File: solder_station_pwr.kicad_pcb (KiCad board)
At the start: 2 copper layers, 82.8 x 69.1 mm, 31 parts, among them J1 PWR_MAIN_LINE, J2 FB_OUT, J3 Conn_01x04, J4 FB_IN, J6 Conn_01x03, Q3 2SD669, T1 RingTrafo_40U, T2 220V-7V5, U2 L7805, U8 LT1073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

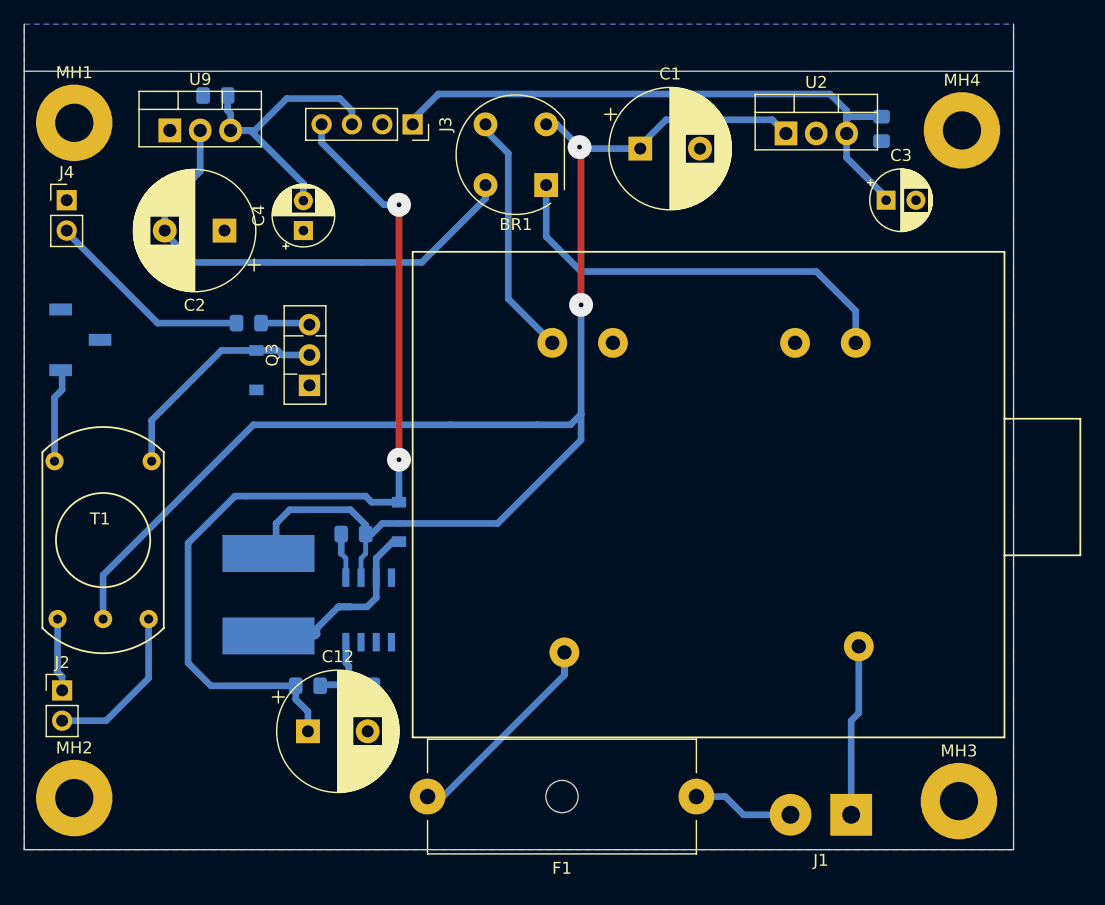
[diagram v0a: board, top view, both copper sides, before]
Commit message: add lm4871 as filament heater
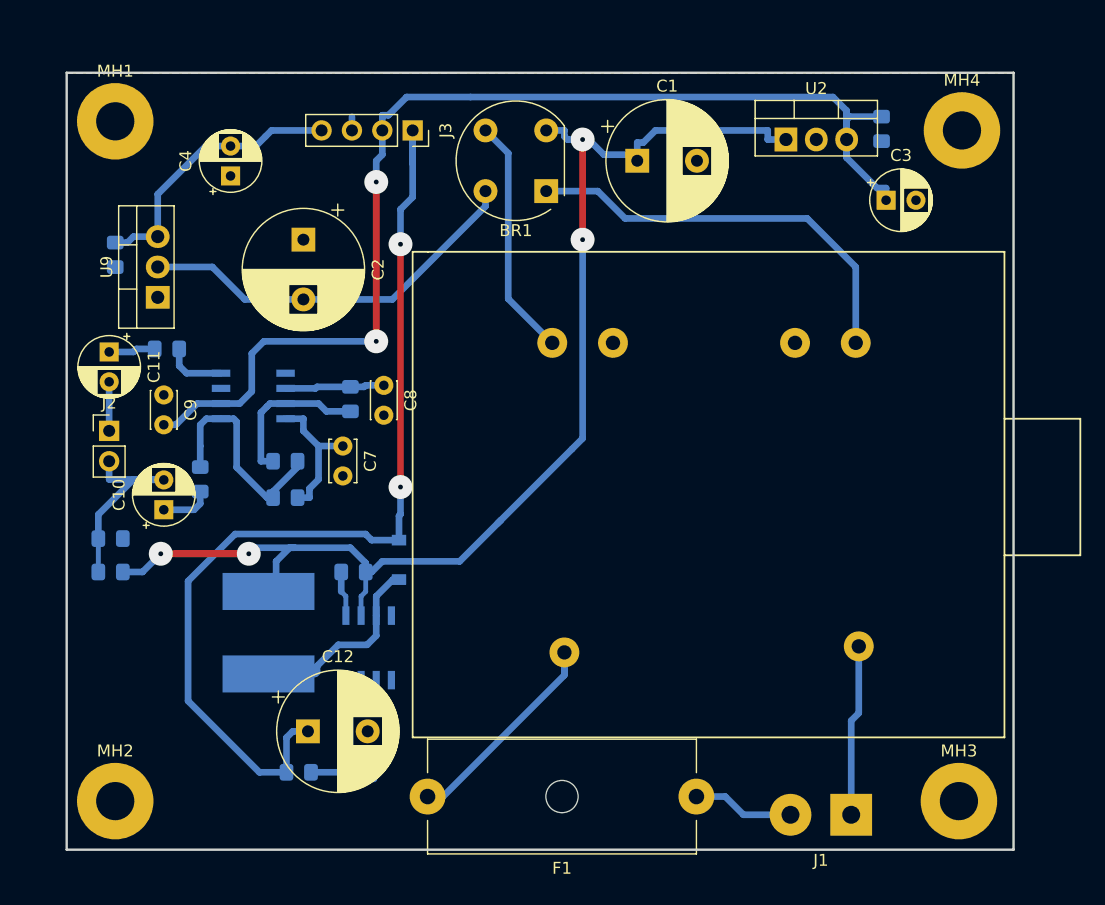
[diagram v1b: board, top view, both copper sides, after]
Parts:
- removed D2: SD103BW, Diode_SMD:D_SOD-123
- removed J4: FB_IN, Connector_PinHeader_2.54mm:PinHeader_1x02_P2.54mm_Vertical
- removed J6: Conn_01x03, Connector_PinSocket_2.54mm:PinSocket_1x03_P2.54mm_Vertical_SMD_Pin1Left
- removed Q3: 2SD669, Package_TO_SOT_THT:TO-126-3_Vertical
- removed T1: RingTrafo_40U, custom:Transformer_toroid_v_18mm
- added C10: 47u, Capacitor_THT:CP_Radial_D5.0mm_P2.50mm, F.Cu at (51.3, 58.4)
- added C11: 47u, Capacitor_THT:CP_Radial_D5.0mm_P2.50mm, F.Cu at (46.7, 45.2)
- added C7: 4700p, Capacitor_THT:C_Disc_D3.4mm_W2.1mm_P2.50mm, F.Cu at (66.3, 53.1)
- added C8: 1u, Capacitor_THT:C_Disc_D3.0mm_W2.0mm_P2.50mm, F.Cu at (69.7, 48.0)
- added C9: 1u, Capacitor_THT:C_Disc_D3.0mm_W2.0mm_P2.50mm, F.Cu at (51.3, 48.8)
- added R1: 47k, Resistor_SMD:R_0805_2012Metric_Pad1.15x1.40mm_HandSolder, B.Cu at (61.5, 57.4)
- added R2: 10k, Resistor_SMD:R_0805_2012Metric_Pad1.15x1.40mm_HandSolder, B.Cu at (66.9, 49.2)
- added R4: 18, Resistor_SMD:R_0805_2012Metric_Pad1.15x1.40mm_HandSolder, B.Cu at (54.4, 55.9)
- added R5: 18, Resistor_SMD:R_0805_2012Metric_Pad1.15x1.40mm_HandSolder, B.Cu at (51.6, 45.0)
- added R6: 47k, Resistor_SMD:R_0805_2012Metric_Pad1.15x1.40mm_HandSolder, B.Cu at (46.9, 60.8)
- added R7: 4k7, Resistor_SMD:R_0805_2012Metric_Pad1.15x1.40mm_HandSolder, B.Cu at (46.9, 63.6)
- added U1: LM4871, Package_SO:SOIC-8_3.9x4.9mm_P1.27mm, B.Cu at (58.8, 48.9)
- R3: value 1k -> 22k
- moved J2 22.1 mm to (46.7, 51.8)
- moved C6 15.8 mm to (47.2, 37.1), turned to 90 degrees
- moved U9 14.0 mm to (50.8, 40.6), turned to 90 degrees
- moved R3 12.0 mm to (61.5, 54.4)
- moved C4 7.62 mm to (56.9, 30.5)
- moved R25 7.37 mm to (67.6, 80.5)
- moved R24 7.28 mm to (62.6, 80.4)
- moved C2 6.65 mm to (63.0, 35.8), turned to 270 degrees
- moved MH2 3.44 mm to (47.2, 82.8)
- moved MH1 3.43 mm to (47.2, 25.9)
- moved R22 3.18 mm to (67.2, 63.6)
- moved D6 3.17 mm to (71.0, 62.6)
- moved L1 3.17 mm to (60.1, 68.7)
- moved U8 3.17 mm to (68.5, 70.0)
- moved C1 1.05 mm to (90.9, 29.2)
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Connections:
- J2 pad 1: /FB1 -> Net-(C11-Pad2)
- J2 pad 2: /FB2 -> Net-(C10-Pad2)
- J3 pad 1: +5V -> +36V
- J3 pad 2: GND -> +5V
- J3 pad 3: -5V -> GND
- J3 pad 4: +36V -> -5V
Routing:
- net +5V: track 53.1 -> 99.2 mm, vias 0 -> 2
- net /UNR_5V: track 133.2 -> 109.1 mm, vias 2 -> 4
- net Net-(D2-Pad1): track 19.2 -> 0.00 mm
- net Net-(C10-Pad2): track 0.00 -> 17.6 mm
- net Net-(R1-Pad2): track 4.11 -> 20.3 mm
- net /FB2: track 13.7 -> 0.00 mm
- net Net-(C7-Pad1): track 0.00 -> 12.0 mm
- net +36V: track 78.6 -> 87.0 mm
- net Net-(C8-Pad1): track 0.00 -> 8.33 mm
- net Net-(J6-Pad1): track 7.94 -> 0.00 mm
- net Net-(BR1-Pad4): track 41.0 -> 33.6 mm
- net /FB1: track 6.13 -> 0.00 mm
- net Net-(R5-Pad2): track 0.00 -> 5.18 mm
- net Net-(C10-Pad1): track 0.00 -> 4.27 mm
- net Net-(R2-Pad2): track 17.5 -> 13.4 mm
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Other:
- board size 82.8 x 69.1 mm -> 79.2 x 65 mm

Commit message: version
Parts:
- C7: footprint Capacitor_THT:C_Disc_D3.4mm_W2.1mm_P2.50mm -> Capacitor_THT:C_Disc_D4.3mm_W1.9mm_P5.00mm
- C8, C9: footprint Capacitor_THT:C_Disc_D3.0mm_W2.0mm_P2.50mm -> Capacitor_THT:C_Disc_D4.3mm_W1.9mm_P5.00mm
- moved C9 0.94 mm to (51.2, 47.9)
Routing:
- net +5V: track 99.2 -> 100.9 mm
